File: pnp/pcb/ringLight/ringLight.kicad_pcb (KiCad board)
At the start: 2 copper layers, 39.8 x 48.9 mm, 16 parts, among them J1 Conn_01x03_Male, J2 Conn_01x03_Male

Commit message: Update labels ring light
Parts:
- removed ? (x2): , buzzard_labels
- added svg2mod: G***, label, B.Cu at (0.00, 13.5)
- added svg2mod: G***, label, B.Cu at (0.09, -12.2)
- moved G*** 0.09 mm to (0.12, -16.9)

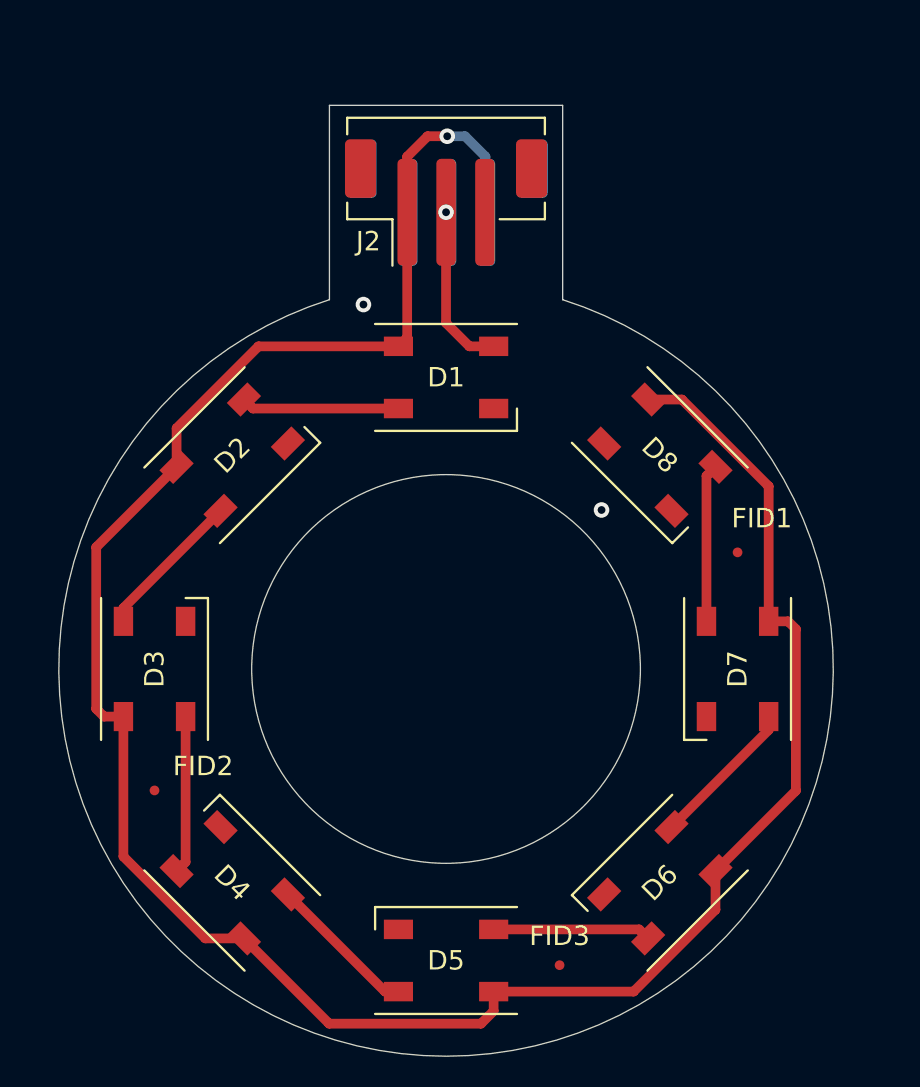
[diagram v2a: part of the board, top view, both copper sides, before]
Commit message: updated ring light to rev03. changed connector pinout to match motherboard. switched to THT for connector that works with both right angle and straight up to be compatible with both board orientations. increased fiducial size. added decoupling capacitor.
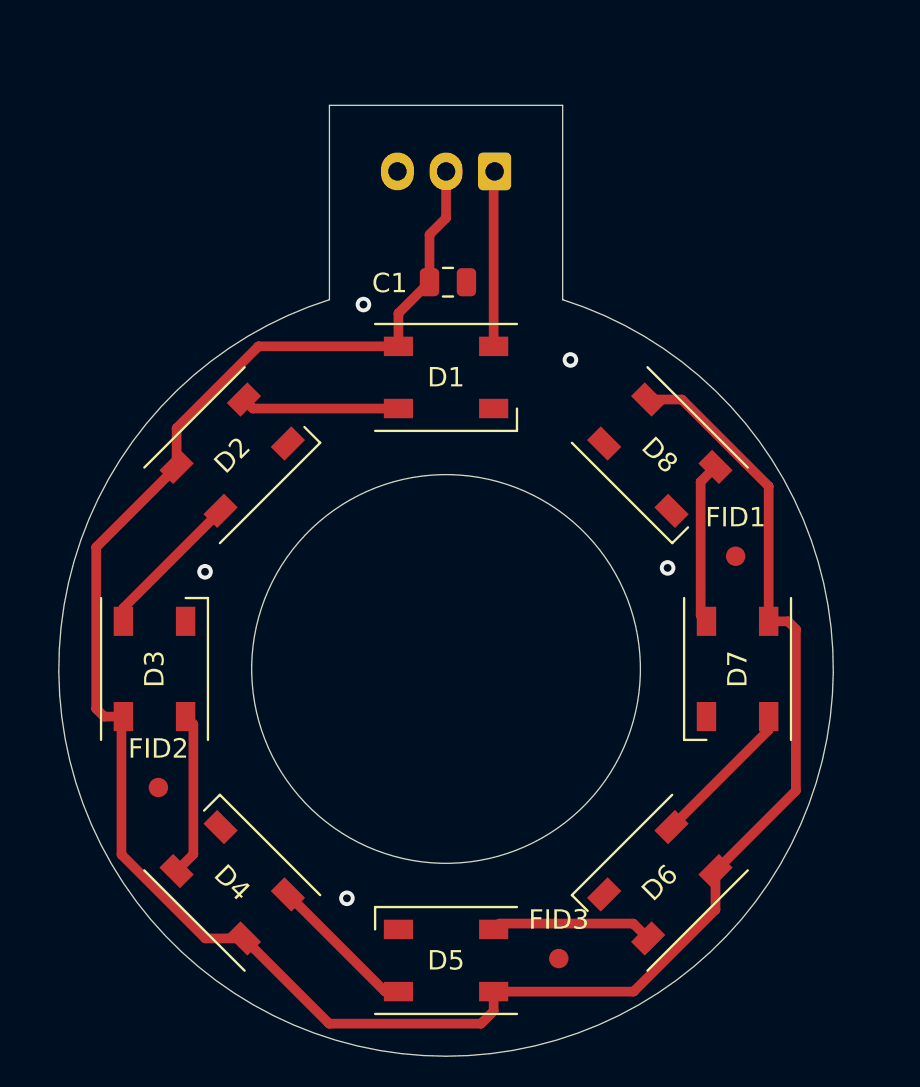
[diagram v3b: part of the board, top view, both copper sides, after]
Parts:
- removed J2: Conn_01x03_Male, Connector_JST:JST_PH_B3B-PH-SM4-TB_1x03-1MP_P2.00mm_Vertical
- removed the svg2mod at (0.00, 13.5)
- added C1: 10uF, Capacitor_SMD:C_0805_2012Metric, F.Cu at (0.10, -19.9)
- FID1, FID2, FID3: footprint Fiducial:Fiducial_0.5mm_Mask1mm -> Fiducial:Fiducial_1mm_Mask2mm
- J1: footprint Connector_JST:JST_PH_B3B-PH-SM4-TB_1x03-1MP_P2.00mm_Vertical -> Connector_JST:JST_XH_B3B-XH-A_1x03_P2.50mm_Vertical
- moved J1 2.95 mm to (2.50, -25.6)
- moved FID3 0.34 mm to (5.80, 14.9)
- moved FID2 0.25 mm to (-14.8, 6.10)
- moved FID1 0.22 mm to (14.9, -5.80)
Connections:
- net Net-(D1-Pad3) renamed GND
- D1 pad 1: Net-(D1-Pad1) -> +5V
- D1 pad 4: Net-(D1-Pad4) -> DIN
- D2 pad 1: Net-(D1-Pad1) -> +5V
- D3 pad 1: Net-(D1-Pad1) -> +5V
- D4 pad 1: Net-(D1-Pad1) -> +5V
- D5 pad 1: Net-(D1-Pad1) -> +5V
- D6 pad 1: Net-(D1-Pad1) -> +5V
- D7 pad 1: Net-(D1-Pad1) -> +5V
- D8 pad 1: Net-(D1-Pad1) -> +5V
- J1 pad 1: Net-(D1-Pad1) -> DIN
- J1 pad 2: Net-(D1-Pad4) -> +5V
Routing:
- net Net-(D1-Pad1): track 125.5 -> 0.00 mm, vias 1 -> 0
- net +5V: track 0.00 -> 118.3 mm
- net DIN: track 0.00 -> 9.74 mm
- net Net-(D1-Pad4): track 8.68 -> 0.00 mm, vias 1 -> 0
- net GND: vias 2 -> 5
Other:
- board text added: "REV03"

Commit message: Fix #377
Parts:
- moved FID2 184.4 mm to (135.6, 112.8)
- moved C1 184.4 mm to (150.5, 86.8)
- moved D1 184.4 mm to (150.4, 91.7)
- moved D2 184.4 mm to (139.4, 95.7)
- moved D3 184.4 mm to (135.4, 106.7)
- moved D4 184.4 mm to (139.4, 117.7)
- moved D5 184.4 mm to (150.4, 121.7)
- moved D6 184.4 mm to (161.4, 117.7)
- moved D7 184.4 mm to (165.4, 106.7)
- moved D8 184.4 mm to (161.4, 95.7)
- moved FID1 184.4 mm to (165.3, 100.9)
- moved FID3 184.4 mm to (156.2, 121.6)
- moved G*** 184.4 mm to (150.6, 89.8)
- moved J1 184.4 mm to (152.9, 81.1)
- moved svg2mod 184.4 mm to (150.5, 94.5)

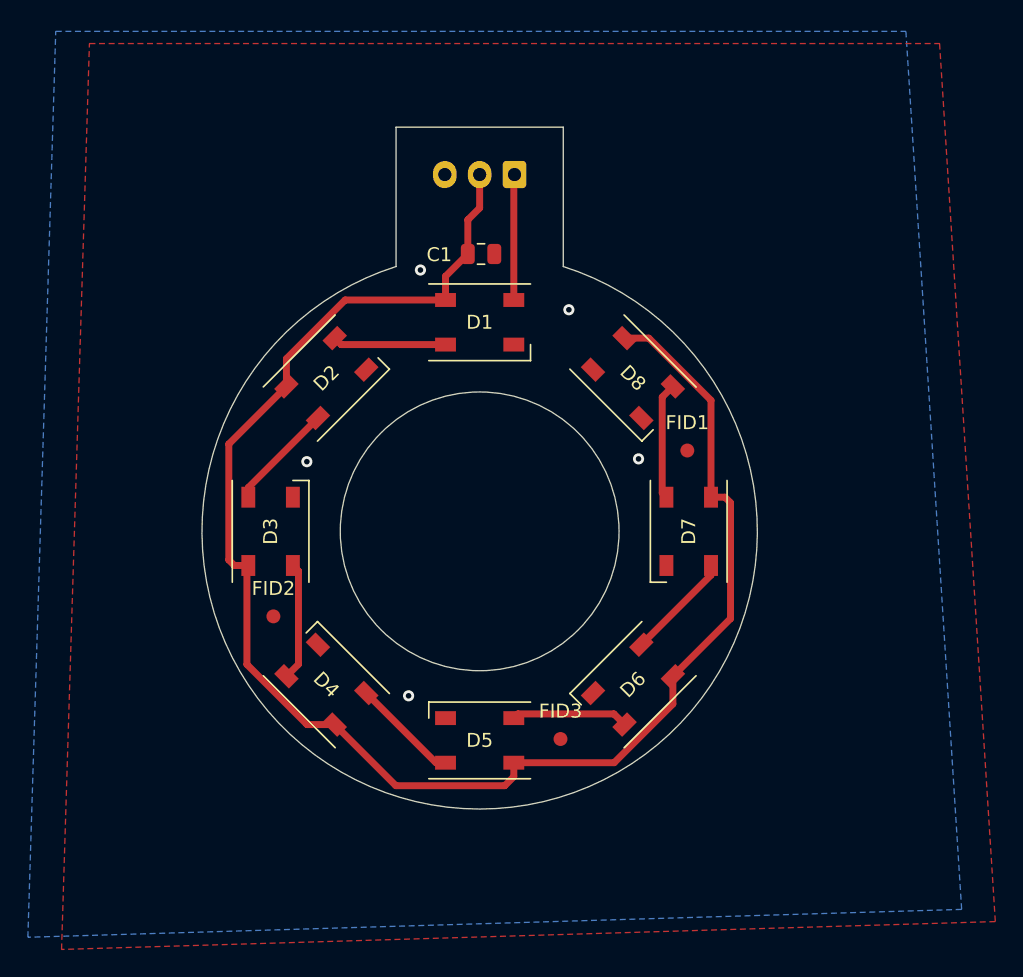
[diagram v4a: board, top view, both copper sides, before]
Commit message: Ring Light Rev 04 - new schematic and pcb
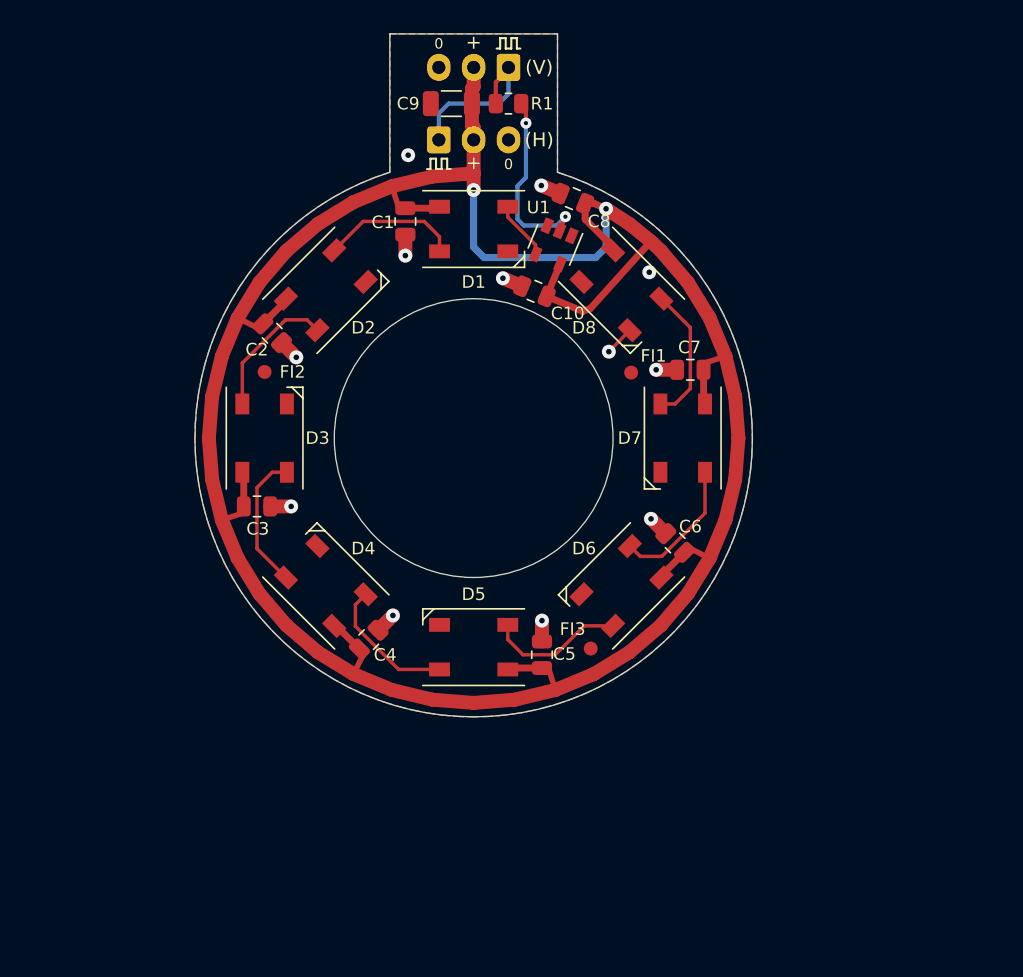
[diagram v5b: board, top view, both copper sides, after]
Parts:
- added C10: 100nF, Capacitor_SMD:C_0805_2012Metric, F.Cu at (154.4, 89.5)
- added C2: 100nF, Capacitor_SMD:C_0805_2012Metric, F.Cu at (135.5, 92.5)
- added C3: 100nF, Capacitor_SMD:C_0805_2012Metric, F.Cu at (134.5, 104.9)
- added C4: 100nF, Capacitor_SMD:C_0805_2012Metric, F.Cu at (142.5, 114.5)
- added C5: 100nF, Capacitor_SMD:C_0805_2012Metric, F.Cu at (154.9, 115.5)
- added C6: 100nF, Capacitor_SMD:C_0805_2012Metric, F.Cu at (164.5, 107.5)
- added C7: 100nF, Capacitor_SMD:C_0805_2012Metric, F.Cu at (165.5, 95.1)
- added C8: 100nF, Capacitor_SMD:C_0805_2012Metric, F.Cu at (157.1, 82.8)
- added C9: 10uF, Capacitor_SMD:C_1206_3216Metric, F.Cu at (148.4, 76.0)
- added J2: Connector Horizontal, Connector_JST:JST_XH_S3B-XH-A-1_1x03_P2.50mm_Horizontal, B.Cu at (147.5, 78.6)
- added R1: 330R, Resistor_SMD:R_0805_2012Metric, F.Cu at (152.5, 76.0)
- added U1: 74AHCT1G32, Package_TO_SOT_SMD:SOT-23-5, F.Cu at (155.7, 86.1)
- C1: value 10uF -> 100nF
- J1: value Conn_01x03_Male -> Connector Vertical
- svg2mod: value G*** -> n/a
- moved LOGO 18.6 mm to (135.0, 100.0)
- moved FI2 17.6 mm to (135.0, 95.2)
- moved svg2mod 9.05 mm to (150.0, 85.5)
- moved J1 7.70 mm to (152.5, 73.4)
- moved D6 7.13 mm to (160.6, 110.6)
- moved D4 7.08 mm to (139.4, 110.6)
- moved FI1 6.89 mm to (161.3, 95.3)
- moved FI3 6.84 mm to (158.4, 115.1)
- moved D1 6.70 mm to (150.0, 85.0)
- moved D3 6.70 mm to (135.0, 100.0)
- moved D5 6.70 mm to (150.0, 115.0)
- moved D7 6.70 mm to (165.0, 100.0)
- moved D8 6.35 mm to (160.6, 89.4)
- moved D2 6.30 mm to (139.4, 89.4)
- moved C1 5.91 mm to (145.1, 84.5), turned to 270 degrees
- renumbered FID1 to FI1, FID2 to FI2, FID3 to FI3, G*** to LOGO
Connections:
- D1 pad 4: DIN -> Data_In_5V
- J1 pad 1: DIN -> Data_In_3V3
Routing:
- net +5V: track 118.3 -> 185.4 mm, vias 0 -> 2
- net GND: track 0.00 -> 16.0 mm, vias 5 -> 12
- net Net-(R1-Pad1): track 0.00 -> 13.7 mm, vias 0 -> 2
- net Data_In_3V3: track 0.00 -> 12.4 mm
- net DIN: track 9.74 -> 0.00 mm
- net Data_In_5V: track 0.00 -> 4.22 mm
- net Net-(D4-Pad2): track 7.76 -> 9.92 mm
- net Net-(D2-Pad2): track 7.76 -> 9.92 mm
- net Net-(D6-Pad2): track 7.76 -> 9.92 mm
- net Net-(D1-Pad2): track 8.14 -> 9.92 mm
- net Net-(D5-Pad2): track 8.39 -> 9.92 mm
- net Net-(D7-Pad2): track 8.39 -> 9.92 mm
- net Net-(D3-Pad2): track 8.47 -> 9.92 mm
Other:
- board size 39.8 x 48.9 mm -> 40 x 49 mm
- board text added: "(H)"
- board text added: "(V)"
- board text added: "+"
- board text added: "0"
- board text added: "PCB-0002-04"
- board text removed: "REV03"
